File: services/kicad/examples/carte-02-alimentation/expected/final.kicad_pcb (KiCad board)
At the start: 2 copper layers, 34.8 x 25.3 mm, 12 parts, among them J1 IN_5V, J2 OUT, U1 AMS1117-3.3, U2 AMS1117-1.8

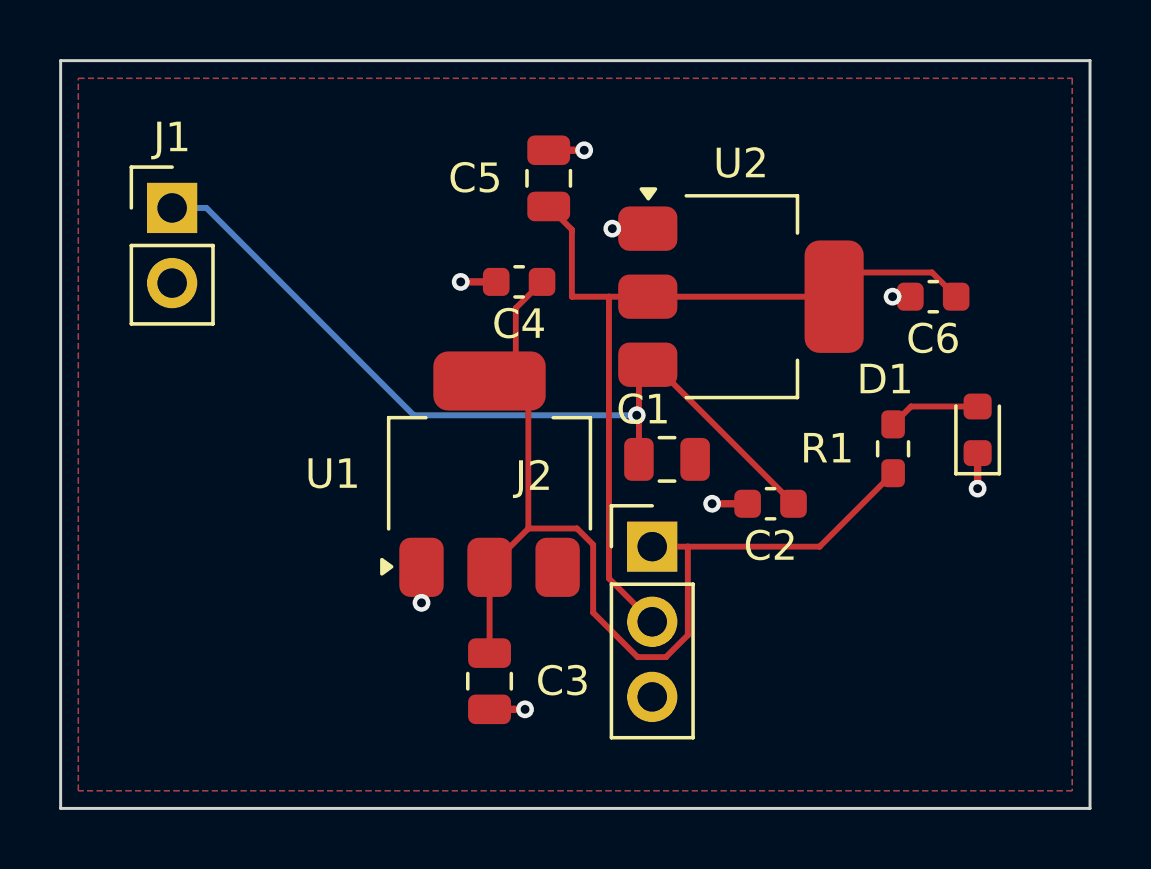
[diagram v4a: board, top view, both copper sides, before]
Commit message: feat(placement): les peripheriques se REPARTISSENT, ils ne s empilent plus
Question de l utilisateur devant le rendu : « c est quoi ce type de placement ? ».
Les composants s entassaient d un seul cote du boitier, etiquettes de
serigraphie l une sur l autre, trois quarts de la couronne vides.

TROIS CAUSES, toutes dans `_poser_les_peripheriques`, toutes la meme faute —
un angle unique pour tout un groupe :

  - les DIRECTS qui visent la meme broche (tous les decouplages d un rail,
    toutes les resistances d un meme signal) recevaient le MEME `angle_vers`
    et le meme rayon de depart ;
  - les SUIVEURS d un meme parent recevaient tous atan2(parent - centre) ;
  - les ISOLES partaient tous de l angle 0.0, c est-a-dire du meme point.

`le_long_du_rayon` ne s ecartait qu une fois la place prise : d ou la file.

REMEDE : `_ecart_en_eventail`. Le PREMIER de chaque groupe garde EXACTEMENT la
direction calculee — c est la topologie, on ne la perd pas pour faire joli — et
les suivants s ecartent symetriquement de 3 x `_PAS_ANGLE_DEG`.
Rien de deja pose ne bouge : seul l ANGLE DE DEPART de la recherche change, et
`le_long_du_rayon` reste seul juge de ce qui est libre.

BANC DES DIX CARTES, contour resserre ET peripheriques repartis :

    carte             demandee    livree         err  manq
    carte-01           25 x 20    20,1 x 13,6     0    0
    carte-02           55 x 40    34,9 x 25,2     0    0
    carte-03           50 x 35    27,6 x 19,9     0    0
    carte-04           60 x 45    36,6 x 29,8     0    0
    carte-05           70 x 50    40,0 x 32,6     0    0
    carte-06           80 x 60    46,5 x 36,4     0    0
    carte-07          110 x 80    47,7 x 38,8     0    0
    carte-08          125 x 95    57,4 x 44,1     0    0
    carte-09          130 x 100   57,8 x 45,2     0    0
    carte-10          140 x 105   59,0 x 45,8     0    0

Dix sur dix, 100 % route. carte-07 gagne 5,5 mm de largeur sur le passage
precedent, carte-06 deux, carte-10 deux. Sur ca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
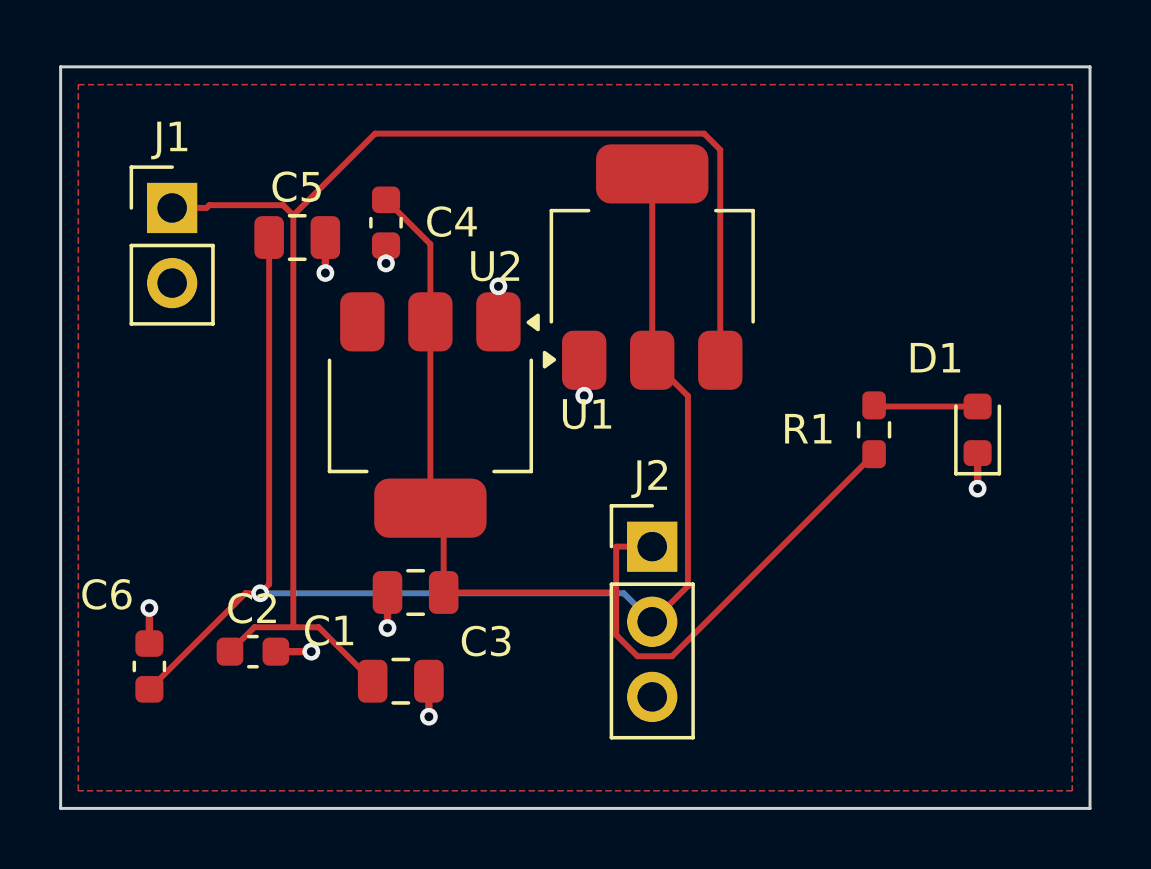
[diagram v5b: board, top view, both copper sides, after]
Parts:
- moved C6 29.3 mm to (124.0, 105.5), turned to 90 degrees
- moved C2 18.2 mm to (127.5, 105.0), turned to 0 degrees
- moved C1 11.7 mm to (132.5, 106.0)
- moved C5 8.73 mm to (129.0, 91.0), turned to 0 degrees
- moved C4 4.92 mm to (132.0, 90.5), turned to -90 degrees
- moved C3 3.91 mm to (133.0, 103.0), turned to 180 degrees
- moved U2 3.16 mm to (141.0, 92.0), turned to 90 degrees
- moved U1 2.83 mm to (133.5, 97.0), turned to -90 degrees
- moved R1 0.91 mm to (148.5, 97.5)
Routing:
- net +1V8: track 28.6 -> 47.0 mm, vias 0 -> 1
- net VIN: track 28.9 -> 47.0 mm, vias 1 -> 0
- net GND: track 9.00 -> 10.2 mm, vias 8 -> 9
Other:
- board size 34.8 x 25.3 mm -> 34.8 x 25.1 mm

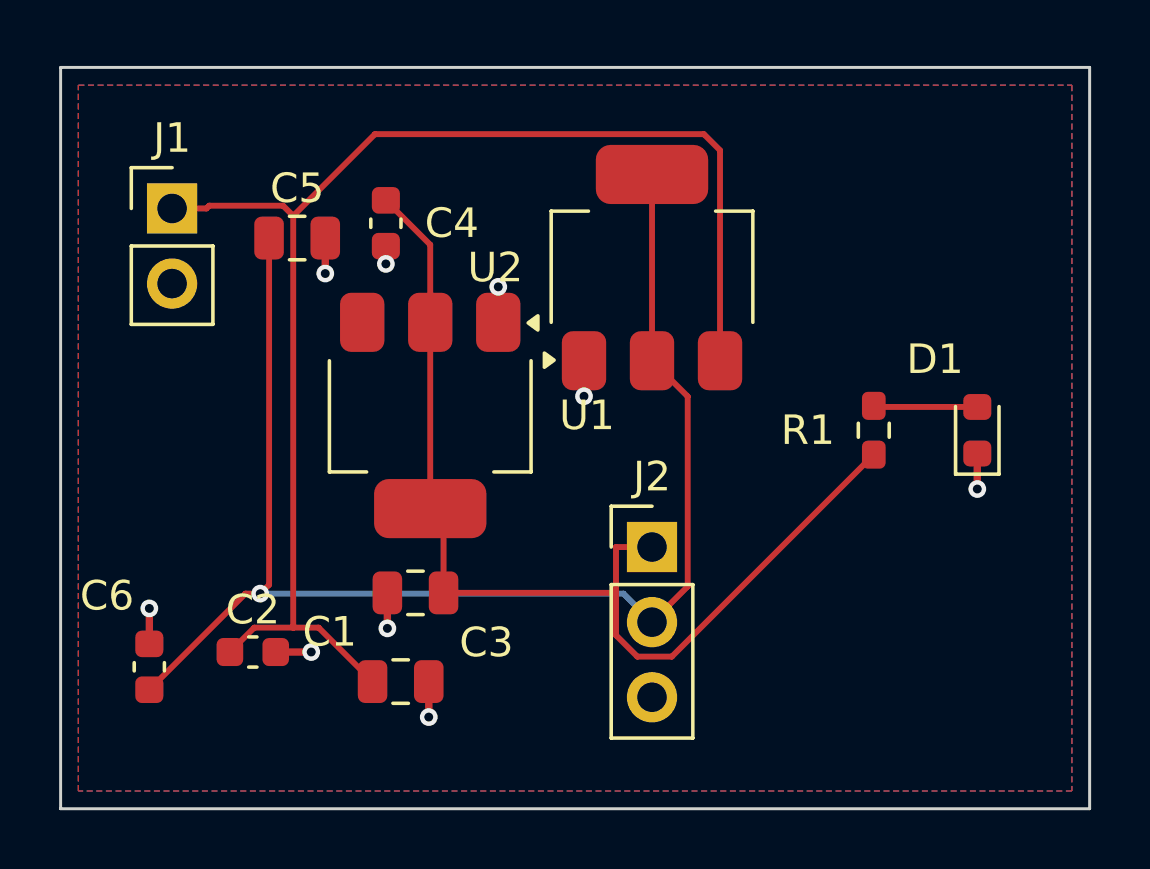
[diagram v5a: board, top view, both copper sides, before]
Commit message: docs(banc): les dix boards du banc du 2026-09-23, service corrige
Artefacts du banc dont le tableau est deja commite : les dix cartes a
100 % route, 0 erreur, 0 connexion manquante, chacune a la taille de son
circuit.

Co-Authored-By: Claude Opus 5 <noreply@anthropic.com>
Claude-Session: https://claude.ai/code/session_01TnMqm4La2CxQHHB5K8aSSV
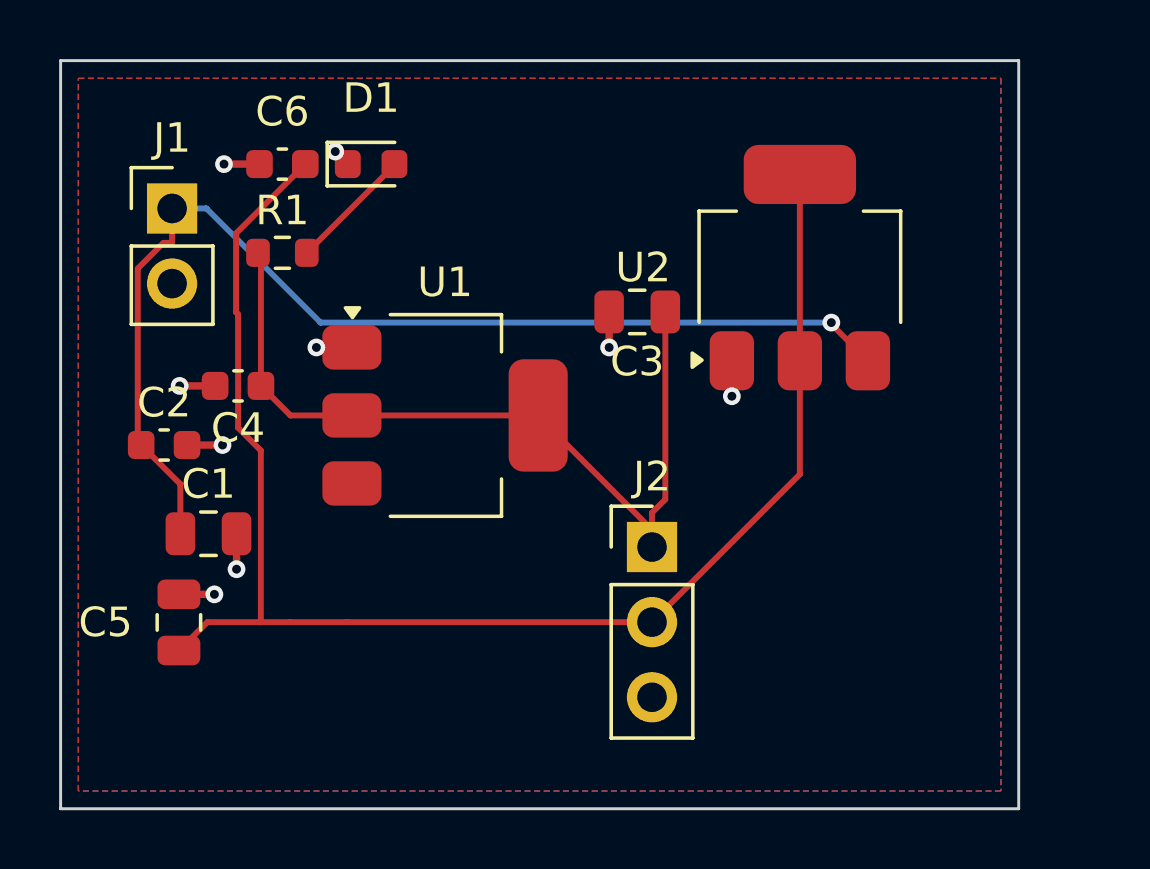
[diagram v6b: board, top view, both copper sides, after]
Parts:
- moved D1 22.4 mm to (131.5, 88.5), turned to 0 degrees
- moved R1 20.9 mm to (128.5, 91.5), turned to 0 degrees
- moved C6 17.6 mm to (128.5, 88.5), turned to 180 degrees
- moved C5 13.6 mm to (125.0, 104.0), turned to 90 degrees
- moved C3 12.1 mm to (140.5, 93.5)
- moved C1 8.20 mm to (126.0, 101.0)
- moved C2 7.62 mm to (124.5, 98.0)
- moved C4 7.43 mm to (127.0, 96.0), turned to 180 degrees
- moved U2 5.00 mm to (146.0, 92.0)
- moved U1 0.50 mm to (134.0, 97.0), turned to 0 degrees
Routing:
- net VIN: track 47.0 -> 37.9 mm, vias 0 -> 1
- net +3V3: track 36.0 -> 27.9 mm
- net +1V8: track 47.0 -> 50.7 mm, vias 1 -> 0
- net LED_A: track 3.52 -> 4.23 mm
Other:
- board size 34.8 x 25.1 mm -> 32.4 x 25.3 mm
